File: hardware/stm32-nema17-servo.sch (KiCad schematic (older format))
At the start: 95 parts, among them J1 Conn_01x05, J2 C31-S-RA-CS1A-BK-SS, J3 TC-2050, J4 Screw_Terminal_01x02, J5 Screw_Terminal_01x02, J7 Conn_01x03, J8 Conn_01x03, J9 Conn_01x02, M1 Stepper_Motor_bipolar, Q1 NTTFS4937N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

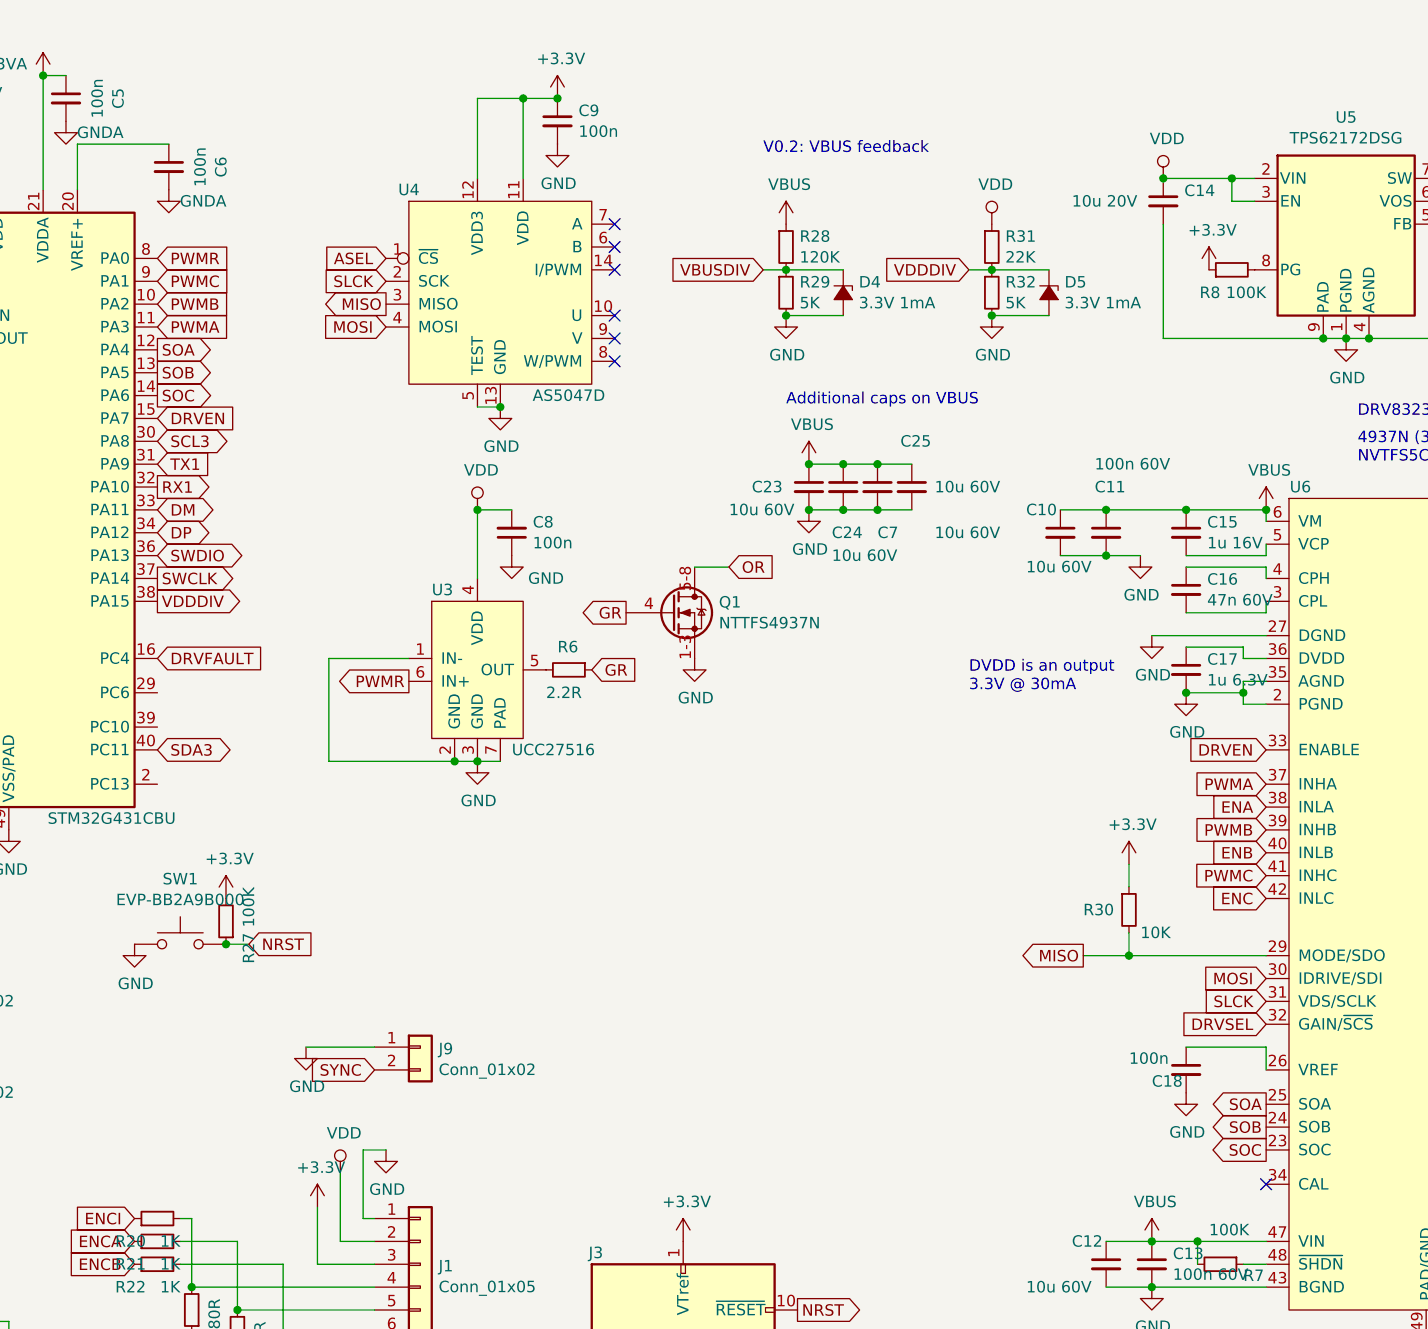
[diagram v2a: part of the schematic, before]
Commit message: adds missing VREF connections on STM32 and DRV8323
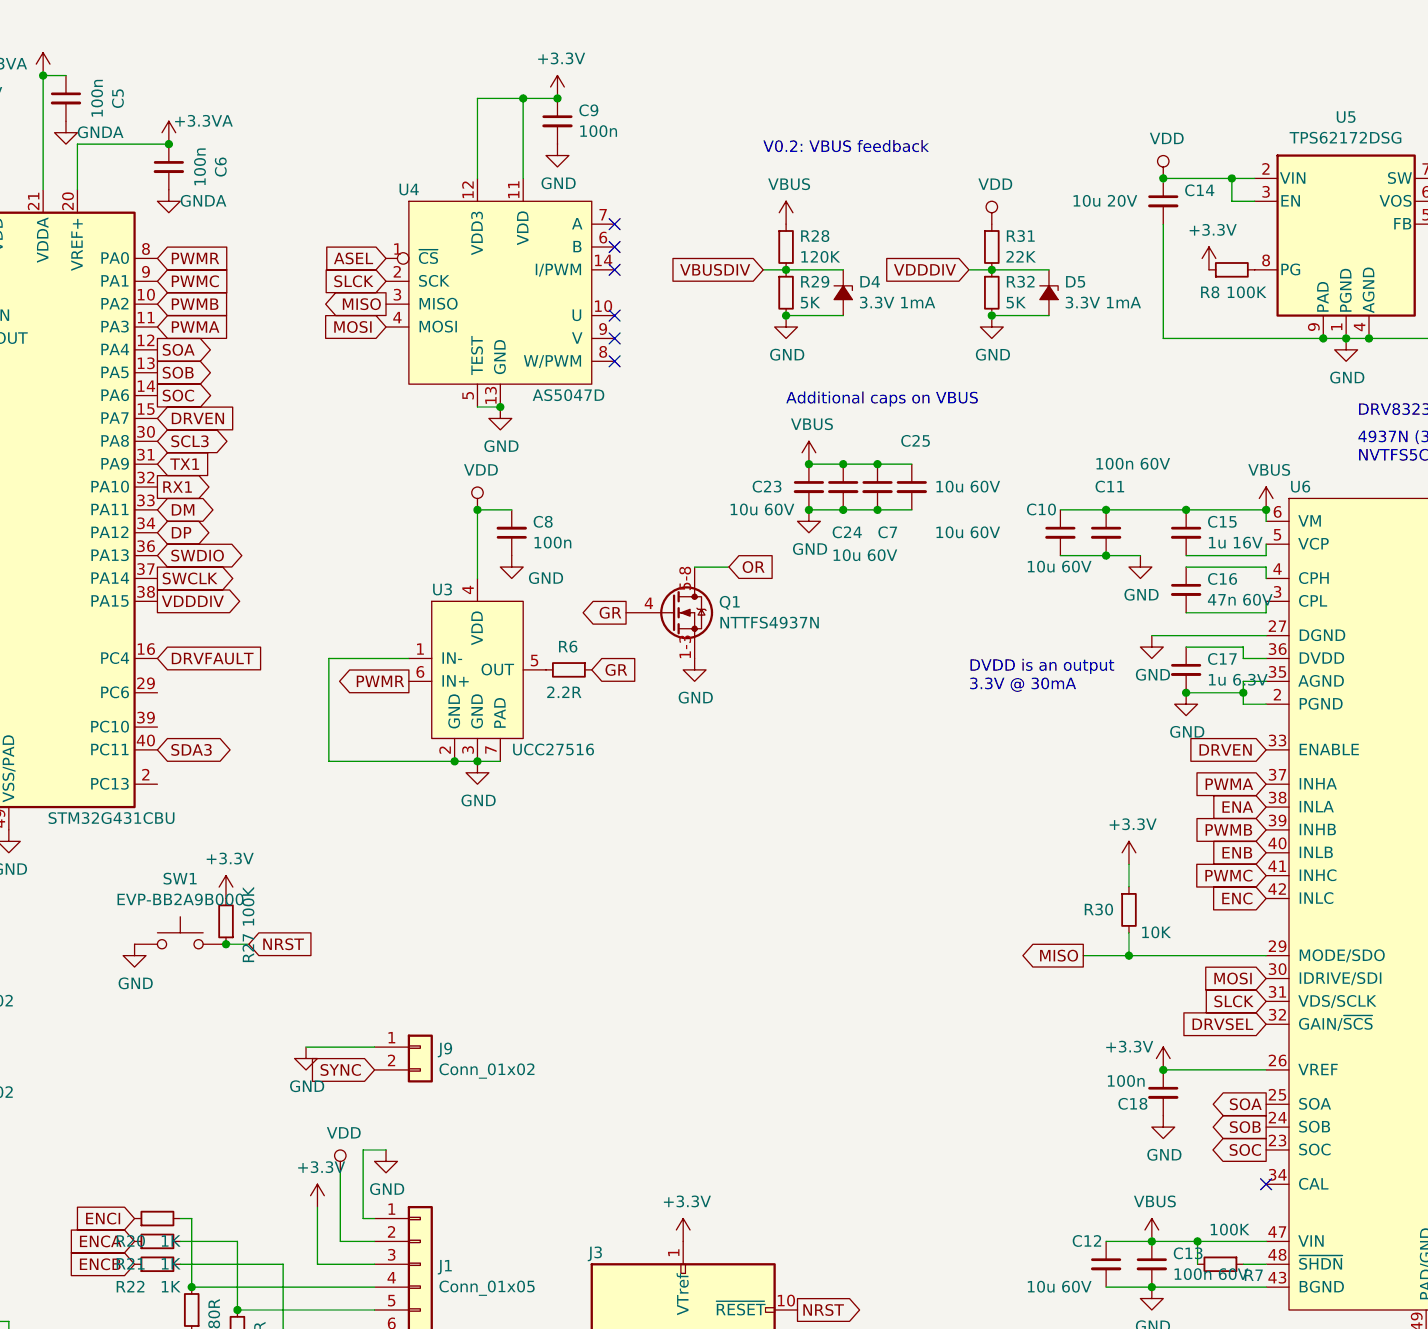
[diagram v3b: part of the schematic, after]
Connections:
- net +3.3VA: now also C6.1, U1.20 (VREF+)
- net +3V3: now also C18.1, U6.26 (VREF)
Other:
- moved on the sheet: C18
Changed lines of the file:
@@
 encoding utf-8
 Sheet 1 1
-Title ""
-Date ""
-Rev ""
-Comp ""
+Title "stm32-nema17-servo"
+Date "2019-09-16"
+Rev "V0.3"
+Comp "InRobCo"
 Comment1 ""
 Comment2 ""
@@
 L Device:C_Small C18
 U 1 1 5D55DE57
-P 7100 5150
-F 0 "C18" H 6950 5100 50  0000 L CNN
-F 1 "100n" H 6850 5200 50  0000 L CNN
-F 2 "Capacitor_SMD:C_0402_1005Metric" H 7100 5150 50  0001 C CNN
-F 3 "~" H 7100 5150 50  0001 C CNN
-	1    7100 5150
-	1    0    0    -1
-$EndComp
-Wire Wire Line
-	7100 5050 7450 5050
-Wire Wire Line
-	7450 5050 7450 5150
+P 7000 5250
+F 0 "C18" H 6800 5200 50  0000 L CNN
+F 1 "100n" H 6750 5300 50  0000 L CNN
+F 2 "Capacitor_SMD:C_0402_1005Metric" H 7000 5250 50  0001 C CNN
+F 3 "~" H 7000 5250 50  0001 C CNN
+	1    7000 5250
+	1    0    0    -1
+$EndComp
 $Comp
 L power:GND #PWR039
 U 1 1 5D561343
-P 7100 5250
-F 0 "#PWR039" H 7100 5000 50  0001 C CNN
-F 1 "GND" H 7105 5077 50  0000 C CNN
-F 2 "" H 7100 5250 50  0001 C CNN
-F 3 "" H 7100 5250 50  0001 C CNN
-	1    7100 5250
+P 7000 5350
+F 0 "#PWR039" H 7000 5100 50  0001 C CNN
+F 1 "GND" H 7005 5177 50  0000 C CNN
+F 2 "" H 7000 5350 50  0001 C CNN
+F 3 "" H 7000 5350 50  0001 C CNN
+	1    7000 5350
 	1    0    0    -1
 $EndComp
@@
 	5750 2700 5900 2700
 Connection ~ 5750 2700
+$Comp
+L power:+3.3V #PWR0111
+U 1 1 5E0BC78F
+P 7000 5150
+F 0 "#PWR0111" H 7000 5000 50  0001 C CNN
+F 1 "+3.3V" H 6850 5250 50  0000 C CNN
+F 2 "" H 7000 5150 50  0001 C CNN
+F 3 "" H 7000 5150 50  0001 C CNN
+	1    7000 5150
+	1    0    0    -1
+$EndComp
+Connection ~ 7000 5150
+Wire Wire Line
+	7000 5150 7450 5150
+$Comp
+L power:+3.3VA #PWR?
+U 1 1 5E11C0E0
+P 2650 1100
+F 0 "#PWR?" H 2650 950 50  0001 C CNN
+F 1 "+3.3VA" H 2800 1200 50  0000 C CNN
+F 2 "" H 2650 1100 50  0001 C CNN
+F 3 "" H 2650 1100 50  0001 C CNN
+	1    2650 1100
+	1    0    0    -1
+$EndComp
+Connection ~ 2650 1100
 $EndSCHEMATC

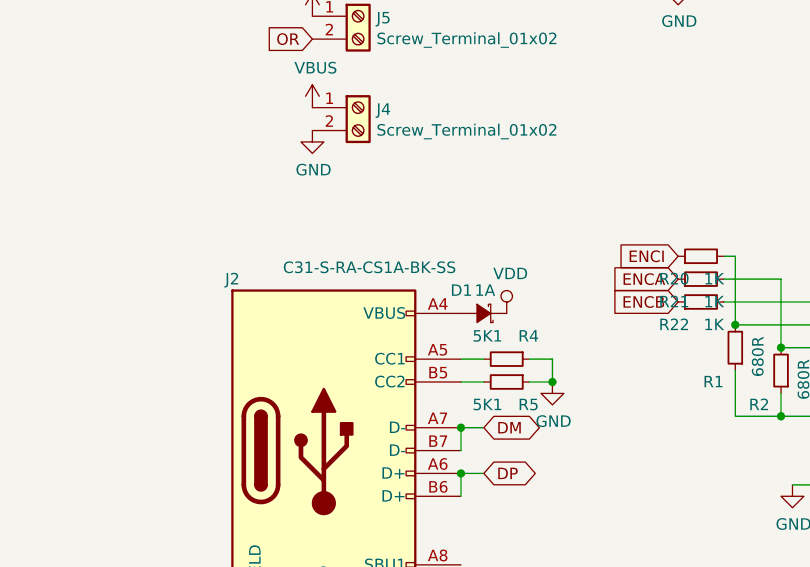
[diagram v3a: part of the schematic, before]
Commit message: adds fuse to USB power input to protect both host and device
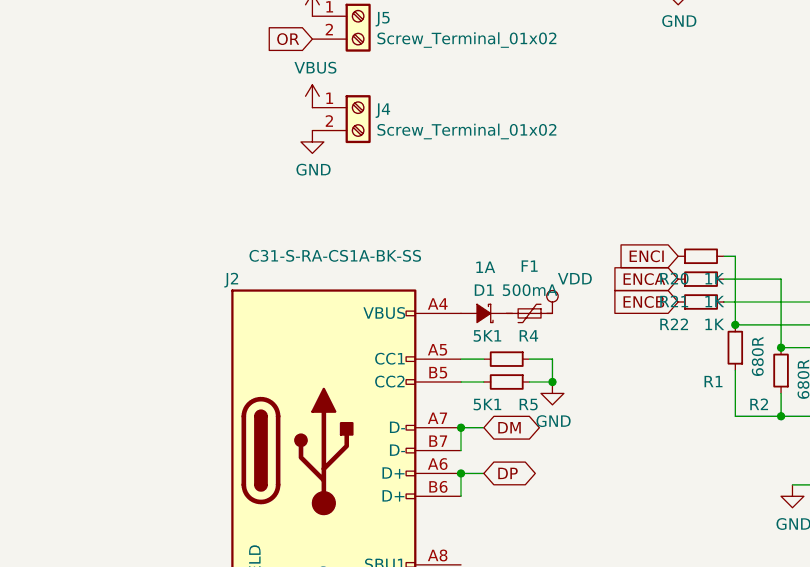
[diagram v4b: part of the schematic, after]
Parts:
- added F1: 500mA, Fuse:Fuse_1206_3216Metric, symbol Device:Polyfuse_Small
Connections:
- net VDD: now also F1.1; no longer D1.1 (K)
- new net: D1.1 (K), F1.2
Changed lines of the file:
@@
 P 950 6650
 F 0 "J2" H 550 7400 50  0000 C CNN
-F 1 "C31-S-RA-CS1A-BK-SS" H 1150 7450 50  0000 C CNN
+F 1 "C31-S-RA-CS1A-BK-SS" H 1000 7500 50  0000 C CNN
 F 2 "stm32-nema17:USB_C_Receptacle_Adam_C31-S-RA-CS1A-BK-SS" H 1100 6650 50  0001 C CNN
 F 3 "https://www.usb.org/sites/default/files/documents/usb_type-c.zip" H 1100 6650 50  0001 C CNN
@@
 U 1 1 5D69E1C8
 P 1650 6050
-F 0 "D1" H 1700 5950 50  0000 L CNN
-F 1 "1A" H 1600 5950 50  0000 L CNN
+F 0 "D1" H 1600 5950 50  0000 L CNN
+F 1 "1A" H 1600 5850 50  0000 L CNN
 F 2 "Diode_SMD:D_0402_1005Metric" V 1650 6050 50  0001 C CNN
 F 3 "~" V 1650 6050 50  0001 C CNN
@@
 L power:VDD #PWR014
 U 1 1 5D6A0CC3
-P 1750 6050
-F 0 "#PWR014" H 1750 5900 50  0001 C CNN
-F 1 "VDD" H 1767 6223 50  0000 C CNN
-F 2 "" H 1750 6050 50  0001 C CNN
-F 3 "" H 1750 6050 50  0001 C CNN
-	1    1750 6050
+P 1950 6050
+F 0 "#PWR014" H 1950 5900 50  0001 C CNN
+F 1 "VDD" H 2050 6200 50  0000 C CNN
+F 2 "" H 1950 6050 50  0001 C CNN
+F 3 "" H 1950 6050 50  0001 C CNN
+	1    1950 6050
 	1    0    0    -1
 $EndComp
@@
 	7000 5150 7450 5150
 $Comp
-L power:+3.3VA #PWR?
+L power:+3.3VA #PWR017
 U 1 1 5E11C0E0
 P 2650 1100
-F 0 "#PWR?" H 2650 950 50  0001 C CNN
+F 0 "#PWR017" H 2650 950 50  0001 C CNN
 F 1 "+3.3VA" H 2800 1200 50  0000 C CNN
 F 2 "" H 2650 1100 50  0001 C CNN
@@
 $EndComp
 Connection ~ 2650 1100
+$Comp
+L Device:Polyfuse_Small F1
+U 1 1 5E23DECB
+P 1850 6050
+F 0 "F1" V 1645 6050 50  0000 C CNN
+F 1 "500mA" V 1750 6050 50  0000 C CNN
+F 2 "Fuse:Fuse_1206_3216Metric" H 1900 5850 50  0001 L CNN
+F 3 "~" H 1850 6050 50  0001 C CNN
+F 4 "0ZCJ0050FF2G" V 1850 6050 50  0001 C CNN "MPN"
+	1    1850 6050
+	0    1    1    0
+$EndComp
 $EndSCHEMATC

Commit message: software updated for V0.2 hardware, with characterization experiments; work on V0.3 hardware fixes
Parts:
- D3: symbol Device:LED_RGBA -> Device:LED_ABRG
- L2: footprint stm32-nema17:L_0806_2016Metric -> Inductor_SMD:L_1008_2520Metric
- R29, R32: value 5K -> 5.1K
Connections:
- net LEDB: now also R15.2, U1.44 (PB6); no longer R14.2, U1.46 (PB8/BOOT0)
- net LEDG: now also R14.2, U1.46 (PB8/BOOT0); no longer R15.2, U1.44 (PB6)
- net VDD: now also D3.1 (A); no longer D3.4 (A)
- net at R17.1: now also D3.4 (GK); no longer D3.1 (RK)
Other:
- moved on the sheet: Q10, Q8, Q9, R14, R15, R16, R17, R18, R19
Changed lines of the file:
@@
 EESchema Schematic File Version 4
-LIBS:stm32-nema17-servo-cache
 EELAYER 30 0
 EELAYER END
@@
 Text GLabel 3600 1700 0    50   Input ~ 0
 SLCK
-Text GLabel 2600 3350 2    50   Input ~ 0
+Text GLabel 2600 3350 2    50   Output ~ 0
 DRVFAULT
 Text GLabel 1300 3900 0    50   Input ~ 0
@@
 Text GLabel 1300 3100 0    50   Input ~ 0
 LEDR
+Text GLabel 1300 3200 0    50   Input ~ 0
+LEDG
 Text GLabel 1300 3000 0    50   Input ~ 0
-LEDG
-Text GLabel 1300 3200 0    50   Input ~ 0
 LEDB
 Text Notes 7850 2500 0    50   ~ 0
@@
 F 0 "L2" V 8540 1250 50  0000 C CNN
 F 1 "2.2uH 1.6A" V 8449 1250 50  0000 C CNN
-F 2 "stm32-nema17:L_0806_2016Metric" H 8350 1250 50  0001 C CNN
+F 2 "Inductor_SMD:L_1008_2520Metric" H 8350 1250 50  0001 C CNN
 F 3 "~" H 8350 1250 50  0001 C CNN
 	1    8350 1250
@@
 $EndComp
 $Comp
-L Device:LED_RGBA D3
+L Device:LED_ABRG D3
 U 1 1 5D6BF710
 P -250 1850
@@
 L Device:Q_NMOS_GSD Q8
 U 1 1 5D6CBFB4
-P -1000 1350
-F 0 "Q8" H -794 1396 50  0000 L CNN
-F 1 "SSM3K35CTC" H -794 1305 50  0000 L CNN
-F 2 "Package_TO_SOT_SMD:SOT-883" H -800 1450 50  0001 C CNN
-F 3 "~" H -1000 1350 50  0001 C CNN
-	1    -1000 1350
-	1    0    0    -1
-$EndComp
-$Comp
-L Device:Q_NMOS_GSD Q9
-U 1 1 5D6CD077
 P -1000 1950
-F 0 "Q9" H -794 1996 50  0000 L CNN
+F 0 "Q8" H -794 1996 50  0000 L CNN
 F 1 "SSM3K35CTC" H -794 1905 50  0000 L CNN
 F 2 "Package_TO_SOT_SMD:SOT-883" H -800 2050 50  0001 C CNN
@@
 $EndComp
 $Comp
-L Device:Q_NMOS_GSD Q10
-U 1 1 5D6CE885
+L Device:Q_NMOS_GSD Q9
+U 1 1 5D6CD077
 P -1000 2550
-F 0 "Q10" H -794 2596 50  0000 L CNN
+F 0 "Q9" H -794 2596 50  0000 L CNN
 F 1 "SSM3K35CTC" H -794 2505 50  0000 L CNN
 F 2 "Package_TO_SOT_SMD:SOT-883" H -800 2650 50  0001 C CNN
@@
 	1    0    0    -1
 $EndComp
-Text GLabel -1400 2550 0    50   Input ~ 0
+Text GLabel -1400 1350 0    50   Input ~ 0
 LEDR
 Text GLabel -1400 1950 0    50   Input ~ 0
 LEDG
-Text GLabel -1400 1350 0    50   Input ~ 0
+Text GLabel -1400 2550 0    50   Input ~ 0
 LEDB
 Wire Wire Line
-	-900 1150 -700 1150
+	-900 1750 -700 1750
 Wire Wire Line
 	-450 1150 -450 1650
 Wire Wire Line
-	-900 1750 -700 1750
+	-900 2350 -700 2350
 Wire Wire Line
 	-450 1750 -450 1850
-Wire Wire Line
-	-900 2350 -700 2350
-Wire Wire Line
-	-450 2350 -450 2050
 $Comp
 L power:GND #PWR0102
 U 1 1 5D6E0B5A
-P -900 1550
-F 0 "#PWR0102" H -900 1300 50  0001 C CNN
-F 1 "GND" H -895 1377 50  0000 C CNN
-F 2 "" H -900 1550 50  0001 C CNN
-F 3 "" H -900 1550 50  0001 C CNN
-	1    -900 1550
-	1    0    0    -1
-$EndComp
-$Comp
-L power:GND #PWR0103
-U 1 1 5D6E2E01
 P -900 2150
-F 0 "#PWR0103" H -900 1900 50  0001 C CNN
+F 0 "#PWR0102" H -900 1900 50  0001 C CNN
 F 1 "GND" H -895 1977 50  0000 C CNN
 F 2 "" H -900 2150 50  0001 C CNN
@@
 $EndComp
 $Comp
-L power:GND #PWR0104
-U 1 1 5D6E46E3
+L power:GND #PWR0103
+U 1 1 5D6E2E01
 P -900 2750
-F 0 "#PWR0104" H -900 2500 50  0001 C CNN
+F 0 "#PWR0103" H -900 2500 50  0001 C CNN
 F 1 "GND" H -895 2577 50  0000 C CNN
 F 2 "" H -900 2750 50  0001 C CNN
@@
 L Device:R_Small R18
 U 1 1 5D6F154D
-P -600 1750
-F 0 "R18" V -700 1800 50  0000 L CNN
-F 1 "470R" V -700 1600 50  0000 L CNN
-F 2 "Resistor_SMD:R_0402_1005Metric" H -600 1750 50  0001 C CNN
-F 3 "~" H -600 1750 50  0001 C CNN
-	1    -600 1750
-	0    1    1    0
-$EndComp
-Wire Wire Line
-	-500 1750 -450 1750
-$Comp
-L Device:R_Small R19
-U 1 1 5D6F53C9
 P -600 2350
-F 0 "R19" V -700 2400 50  0000 L CNN
+F 0 "R18" V -700 2400 50  0000 L CNN
 F 1 "470R" V -700 2200 50  0000 L CNN
 F 2 "Resistor_SMD:R_0402_1005Metric" H -600 2350 50  0001 C CNN
@@
 $EndComp
 Wire Wire Line
-	-500 2350 -450 2350
+	-500 1750 -450 1750
 $Comp
 L Device:R_Small R17
 U 1 1 5D6F68CB
-P -600 1150
-F 0 "R17" V -700 1200 50  0000 L CNN
-F 1 "430R" V -700 1000 50  0000 L CNN
-F 2 "Resistor_SMD:R_0402_1005Metric" H -600 1150 50  0001 C CNN
-F 3 "~" H -600 1150 50  0001 C CNN
-	1    -600 1150
+P -600 1750
+F 0 "R17" V -700 1800 50  0000 L CNN
+F 1 "430R" V -700 1600 50  0000 L CNN
+F 2 "Resistor_SMD:R_0402_1005Metric" H -600 1750 50  0001 C CNN
+F 3 "~" H -600 1750 50  0001 C CNN
+	1    -600 1750
 	0    1    1    0
 $EndComp
@@
 L Device:R_Small R14
 U 1 1 5D6F854B
-P -1300 1350
-F 0 "R14" V -1400 1400 50  0000 L CNN
-F 1 "100R" V -1400 1200 50  0000 L CNN
-F 2 "Resistor_SMD:R_0402_1005Metric" H -1300 1350 50  0001 C CNN
-F 3 "~" H -1300 1350 50  0001 C CNN
-	1    -1300 1350
-	0    1    1    0
-$EndComp
-$Comp
-L Device:R_Small R15
-U 1 1 5D6F9831
 P -1300 1950
-F 0 "R15" V -1400 2000 50  0000 L CNN
+F 0 "R14" V -1400 2000 50  0000 L CNN
 F 1 "100R" V -1400 1800 50  0000 L CNN
 F 2 "Resistor_SMD:R_0402_1005Metric" H -1300 1950 50  0001 C CNN
@@
 $EndComp
 $Comp
-L Device:R_Small R16
-U 1 1 5D6FAB70
+L Device:R_Small R15
+U 1 1 5D6F9831
 P -1300 2550
-F 0 "R16" V -1400 2600 50  0000 L CNN
+F 0 "R15" V -1400 2600 50  0000 L CNN
 F 1 "100R" V -1400 2400 50  0000 L CNN
 F 2 "Resistor_SMD:R_0402_1005Metric" H -1300 2550 50  0001 C CNN
@@
 P 5350 1750
 F 0 "R29" H 5409 1796 50  0000 L CNN
-F 1 "5K" H 5409 1705 50  0000 L CNN
+F 1 "5.1K" H 5409 1705 50  0000 L CNN
 F 2 "Resistor_SMD:R_0402_1005Metric" H 5350 1750 50  0001 C CNN
 F 3 "~" H 5350 1750 50  0001 C CNN
@@
 P 6250 1750
 F 0 "R32" H 6309 1796 50  0000 L CNN
-F 1 "5K" H 6309 1705 50  0000 L CNN
+F 1 "5.1K" H 6309 1705 50  0000 L CNN
 F 2 "Resistor_SMD:R_0402_1005Metric" H 6250 1750 50  0001 C CNN
 F 3 "~" H 6250 1750 50  0001 C CNN
@@
 	0    1    1    0
 $EndComp
+Wire Wire Line
+	-500 2050 -450 2050
+Wire Wire Line
+	-500 2050 -500 2350
+$Comp
+L Device:R_Small R16
+U 1 1 5D6FAB70
+P -1300 1350
+F 0 "R16" V -1400 1400 50  0000 L CNN
+F 1 "100R" V -1400 1200 50  0000 L CNN
+F 2 "Resistor_SMD:R_0402_1005Metric" H -1300 1350 50  0001 C CNN
+F 3 "~" H -1300 1350 50  0001 C CNN
+	1    -1300 1350
+	0    1    1    0
+$EndComp
+$Comp
+L Device:R_Small R19
+U 1 1 5D6F53C9
+P -600 1150
+F 0 "R19" V -700 1200 50  0000 L CNN
+F 1 "470R" V -700 1000 50  0000 L CNN
+F 2 "Resistor_SMD:R_0402_1005Metric" H -600 1150 50  0001 C CNN
+F 3 "~" H -600 1150 50  0001 C CNN
+	1    -600 1150
+	0    1    1    0
+$EndComp
+$Comp
+L power:GND #PWR0104
+U 1 1 5D6E46E3
+P -900 1550
+F 0 "#PWR0104" H -900 1300 50  0001 C CNN
+F 1 "GND" H -895 1377 50  0000 C CNN
+F 2 "" H -900 1550 50  0001 C CNN
+F 3 "" H -900 1550 50  0001 C CNN
+	1    -900 1550
+	1    0    0    -1
+$EndComp
+Wire Wire Line
+	-900 1150 -700 1150
+$Comp
+L Device:Q_NMOS_GSD Q10
+U 1 1 5D6CE885
+P -1000 1350
+F 0 "Q10" H -794 1396 50  0000 L CNN
+F 1 "SSM3K35CTC" H -794 1305 50  0000 L CNN
+F 2 "Package_TO_SOT_SMD:SOT-883" H -800 1450 50  0001 C CNN
+F 3 "~" H -1000 1350 50  0001 C CNN
+	1    -1000 1350
+	1    0    0    -1
+$EndComp
 $EndSCHEMATC

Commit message: PCB layout improvements
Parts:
- C1, C18, C2, C20, C21, C3, C4, C5, C6, C8, C9: MPN (none) -> CC0402KRX5R8BB104
- C10, C12, C23, C24, C25, C7: MPN (none) -> C3225X7R1N106M250AC
- C11, C13: MPN (none) -> GRM155R62A104ME14D
- C14, C22: MPN (none) -> TMK212BBJ106KG
- C15, C17: MPN (none) -> CC0603KRX7R7BB105
- C16: MPN (none) -> CGA3E3X7S2A473K080AB
- C19: MPN (none) -> C0805C226M9PACTU
- D1: MPN (none) -> CDBQT140-HF
- D2: value 1A -> 1A 48V; footprint Diode_SMD:D_0402_1005Metric -> Diode_SMD:D_TUMD2; MPN (none) -> MSS1P6-M3/89A
- D3: MPN (none) -> IN-S128TATRGB
- D4, D5: MPN (none) -> CZRQR3V3B-HF
- J2: MPN (none) -> C31-S-RA-CS1A-BK-SS
- L1, L3: MPN (none) -> BLM18PG471SN1D
- L2: MPN (none) -> CIGT252010EH2R2MNE
- L4: MPN (none) -> VLS5045EX-220M
- Q1: value NTTFS4937N -> NVTFS5C658NL; MPN (none) -> NVTFS5C658NL
- Q2, Q3, Q4, Q5, Q6, Q7: MPN (none) -> NVTFS5C658NL
- R1, R2, R3: MPN (none) -> RC0402JR-07680RL
- R10, R11, R9: MPN (none) -> FCSL32R015FER
- R12, R28: MPN (none) -> RC0402FR-07120KL
- R13, R30: MPN (none) -> RC0402FR-0710KL
- R14, R15, R16: MPN (none) -> RC0402FR-07100RL
- R17: MPN (none) -> RC0402FR-07430RL
- R18, R19: MPN (none) -> RC0402FR-07470RL
- R20, R21, R22, R23, R24, R25, R26: MPN (none) -> RC0402FR-071KL
- R27, R7, R8: MPN (none) -> RC0402FR-07100KL
- R29, R32: value 5.1K -> 5K1; MPN (none) -> RC0402FR-075K11L
- R31: MPN (none) -> RC0402FR-0722KL
- R4, R5: MPN (none) -> RC0402FR-075K11L
- R6: MPN (none) -> RC0402FR-072R2L
- SW1: MPN (none) -> EVP-BB2A9B000
